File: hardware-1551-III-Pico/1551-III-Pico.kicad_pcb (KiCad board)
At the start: 2 copper layers, 100 x 100 mm, 85 parts, among them J1 TCBM, J2 Conn_01x02_Pin, J3 JTAG, J4 DC IN, J5 Module_Panel, J6 SD CARD, J7 Conn_01x02_Pin, M1 Mounting, M2 Mounting, M3 Mounting, M4 Mounting, Q1 BSS138, Q2 BSS138, Q3 BSS138, Q4 BSS138, Q5 BSS138, Q6 BSS138, U12 74LS139, U15 74LS00, U19 74HCT165, U3 Pico, U4 KM62256CLP, U5 27C512, U6 6510T, U9 XC9572XL-VQ64

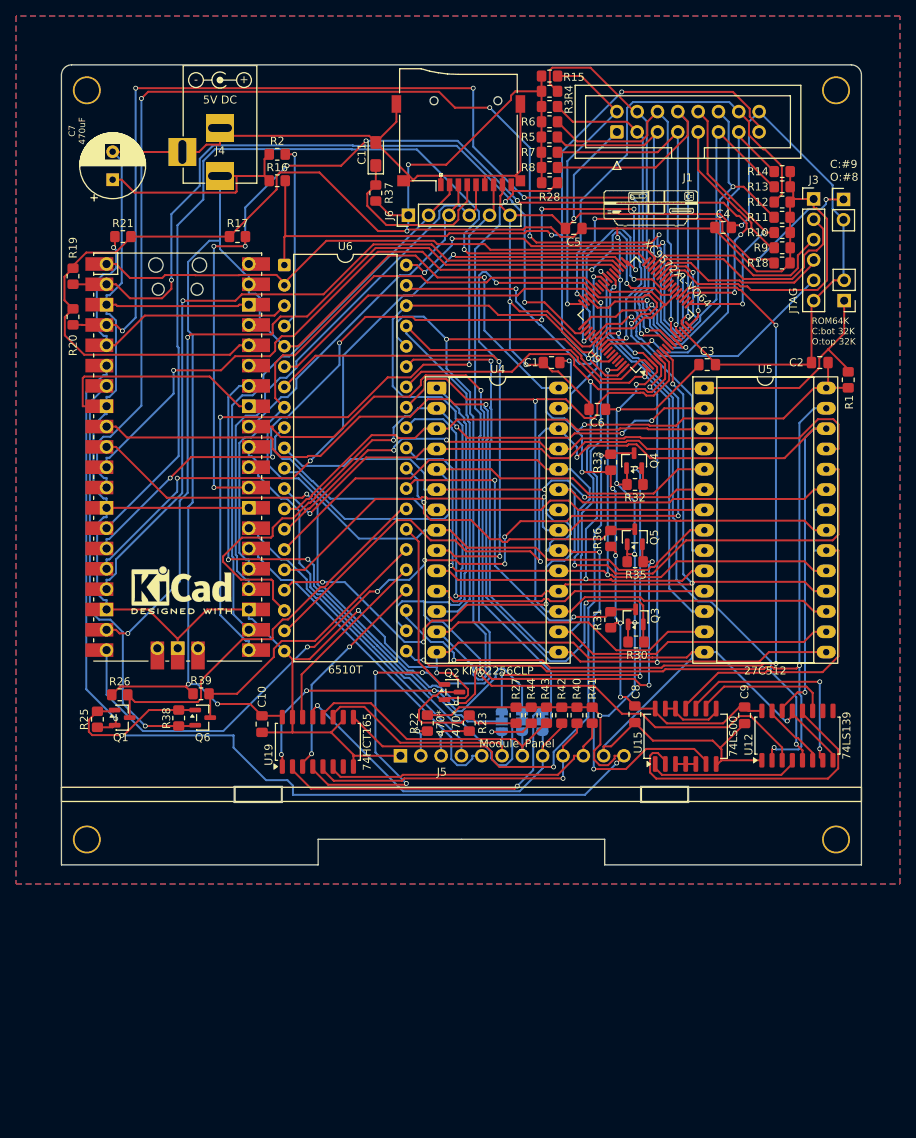
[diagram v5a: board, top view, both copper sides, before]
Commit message: remove '139 and '00 logic to embed it into CPLD, routed final version
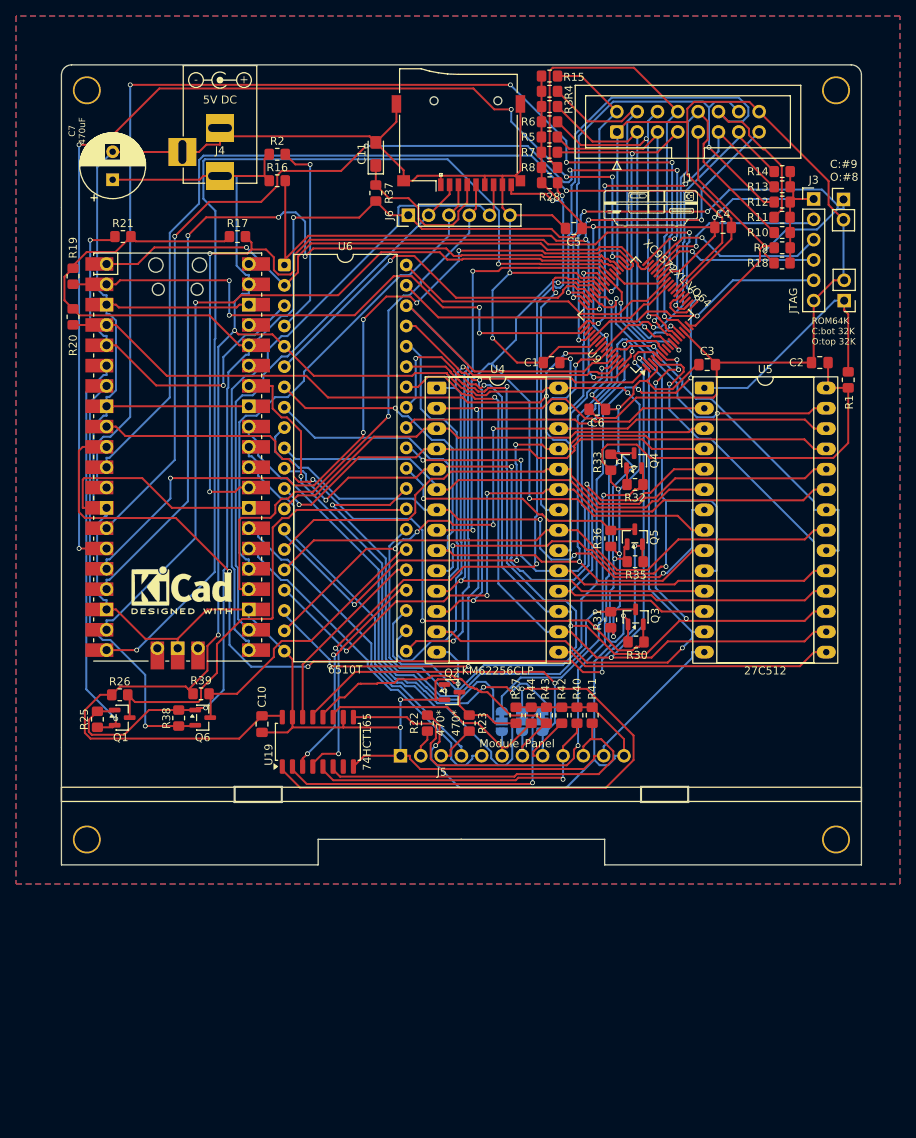
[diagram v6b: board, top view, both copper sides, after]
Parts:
- removed C8, C9: 0.1uF, Capacitor_SMD:C_0805_2012Metric_Pad1.18x1.45mm_HandSolder
- removed U12: 74LS139, Package_SO:SOP-16_4.4x10.4mm_P1.27mm
- removed U15: 74LS00, Package_SO:SO-14_5.3x10.2mm_P1.27mm
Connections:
- U4 pad 22: /~{RAMSEL} -> /~{RAMOE}
- U9 pad 39: /~{CS_TPI} -> /A14
- U9 pad 42: unconnected-(U9-P42-Pad42) -> /~{RAMOE}
- U9 pad 58: unconnected-(U9-P58-Pad58) -> /~{RAMSEL}
- U9 pad 59: unconnected-(U9-P59-Pad59) -> /~{ROMSEL}
- U9 pad 61: unconnected-(U9-P61-Pad61) -> /A13
- U9 pad 62: unconnected-(U9-P62-Pad62) -> /A15
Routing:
- net /~{CS_TPI}: track 74.1 -> 0.00 mm, vias 2 -> 0
- net /SYNC_3V3: track 131.7 -> 74.9 mm, vias 6 -> 2
- net GND: track 594.3 -> 541.1 mm, vias 7 -> 6
- net /~{RAM_HIGH}: track 38.4 -> 0.00 mm
- net /~{RAMOE}: track 0.00 -> 37.9 mm, vias 0 -> 1
- net /A13: track 136.1 -> 99.7 mm, vias 3 -> 5
- net /YB3: track 106.1 -> 140.8 mm, vias 7 -> 6
- net +3V3: track 452.4 -> 421.8 mm, vias 14 -> 11
- net /STP0: track 43.2 -> 71.7 mm
- net /A15: track 97.9 -> 69.7 mm
- net /YB0: track 95.8 -> 123.7 mm, vias 3 -> 1
- net /~{ROM_HIGH}: track 27.1 -> 0.00 mm, vias 2 -> 0
- net /~{RAMSEL}: track 61.1 -> 34.2 mm, vias 2 -> 1
- net /R/~{W}: track 59.9 -> 36.3 mm, vias 2 -> 0
- net /SERIAL_LOAD: track 45.4 -> 68.9 mm, vias 3 -> 1
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
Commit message: rework PCB to be sure that MOS Replacer daughterboard will fit
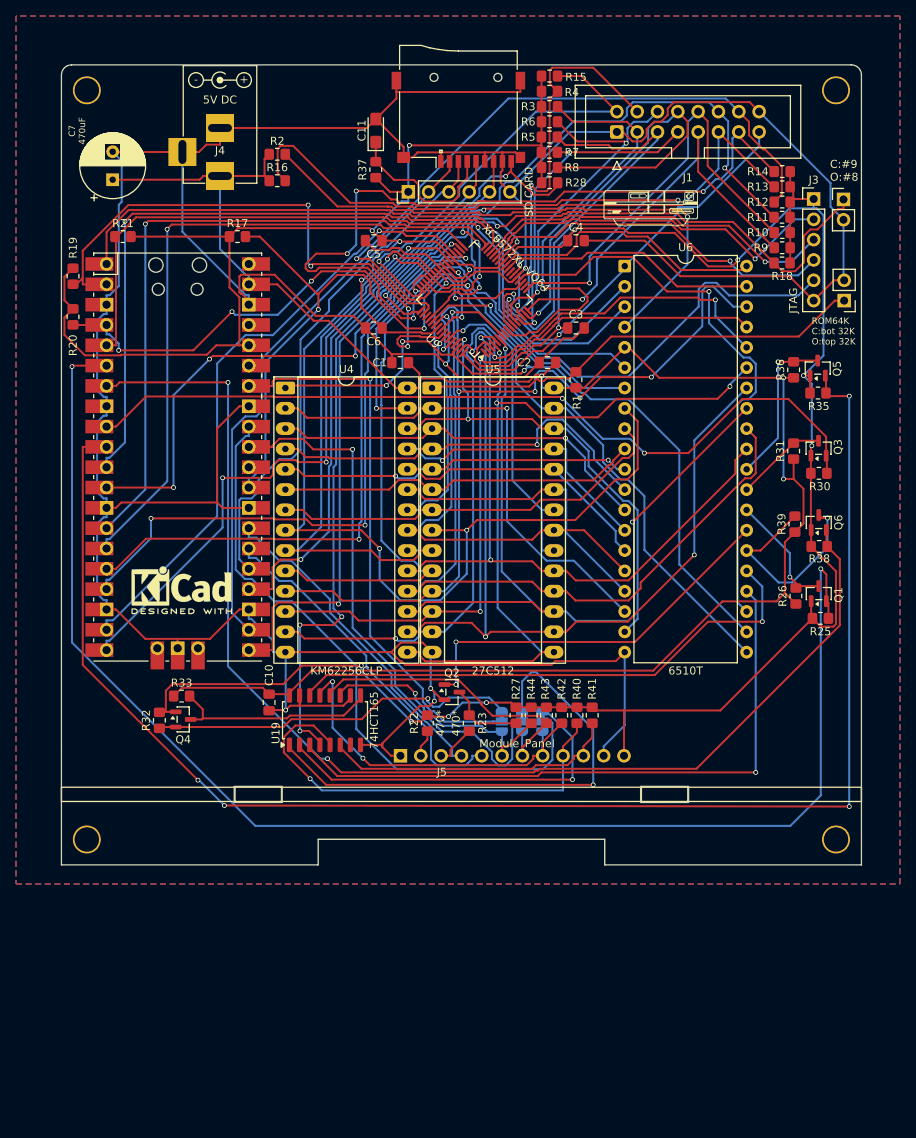
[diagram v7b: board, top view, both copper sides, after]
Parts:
- moved R25 91.3 mm to (165.1, 123.8), turned to 0 degrees
- moved Q1 88.4 mm to (164.8, 120.7), turned to 90 degrees
- moved R26 85.4 mm to (162.0, 121.0), turned to 90 degrees
- moved R38 82.9 mm to (164.9, 114.8), turned to 0 degrees
- moved Q6 80.8 mm to (164.8, 111.8), turned to 90 degrees
- moved R39 77.2 mm to (161.9, 112.0), turned to 90 degrees
- moved R32 66.4 mm to (82.4, 136.5), turned to -90 degrees
- moved Q4 65.0 mm to (85.4, 136.4), turned to 0 degrees
- moved R33 61.1 mm to (85.2, 133.5), turned to 0 degrees
- moved U6 42.5 mm to (140.6, 79.8)
- moved C2 34.0 mm to (130.9, 91.8)
- moved R1 34.0 mm to (134.5, 94.0)
- moved U5 34.0 mm to (116.5, 95.0)
- moved R31 31.1 mm to (161.7, 102.9)
- moved R36 31.1 mm to (161.7, 92.7)
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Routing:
- net /MTR_3V3: track 50.1 -> 178.4 mm, vias 1 -> 2
- net /WPS_3V3: track 53.1 -> 153.1 mm, vias 1 -> 2
- net /STP1_3V3: track 111.8 -> 190.1 mm
- net /YB1: track 142.2 -> 79.4 mm, vias 5 -> 4
- net /ACK: track 43.8 -> 104.3 mm, vias 1 -> 5
- net /STP0: track 71.7 -> 11.5 mm, vias 2 -> 0
- net /YB3: track 140.8 -> 81.7 mm, vias 6 -> 1
- net /A8: track 91.1 -> 34.5 mm, vias 3 -> 1
- net /DS1: track 28.2 -> 80.9 mm, vias 2 -> 1
- net /A11: track 89.0 -> 36.9 mm, vias 3 -> 0
- net /YB7: track 130.7 -> 79.2 mm, vias 2 -> 3
- net /SERIAL_DT: track 77.6 -> 26.2 mm, vias 2 -> 0
- net /~{AEC}: track 25.2 -> 71.3 mm
- net /~{IRQ}: track 48.0 -> 92.4 mm, vias 2 -> 1
- net +5V: track 284.4 -> 240.5 mm, vias 7 -> 3
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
